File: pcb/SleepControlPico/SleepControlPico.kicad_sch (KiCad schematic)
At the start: 24 parts, among them J1 USB_C_Receptacle_PowerOnly_6P, J3 UART, J4 FFC2B35-18-G_REVA2, SW1 RotaryEncoder_Switch, SW2 SW_Push, U1 AMS1117-33, U2 ESP32-WROOM-32D, U3 LIS3DH

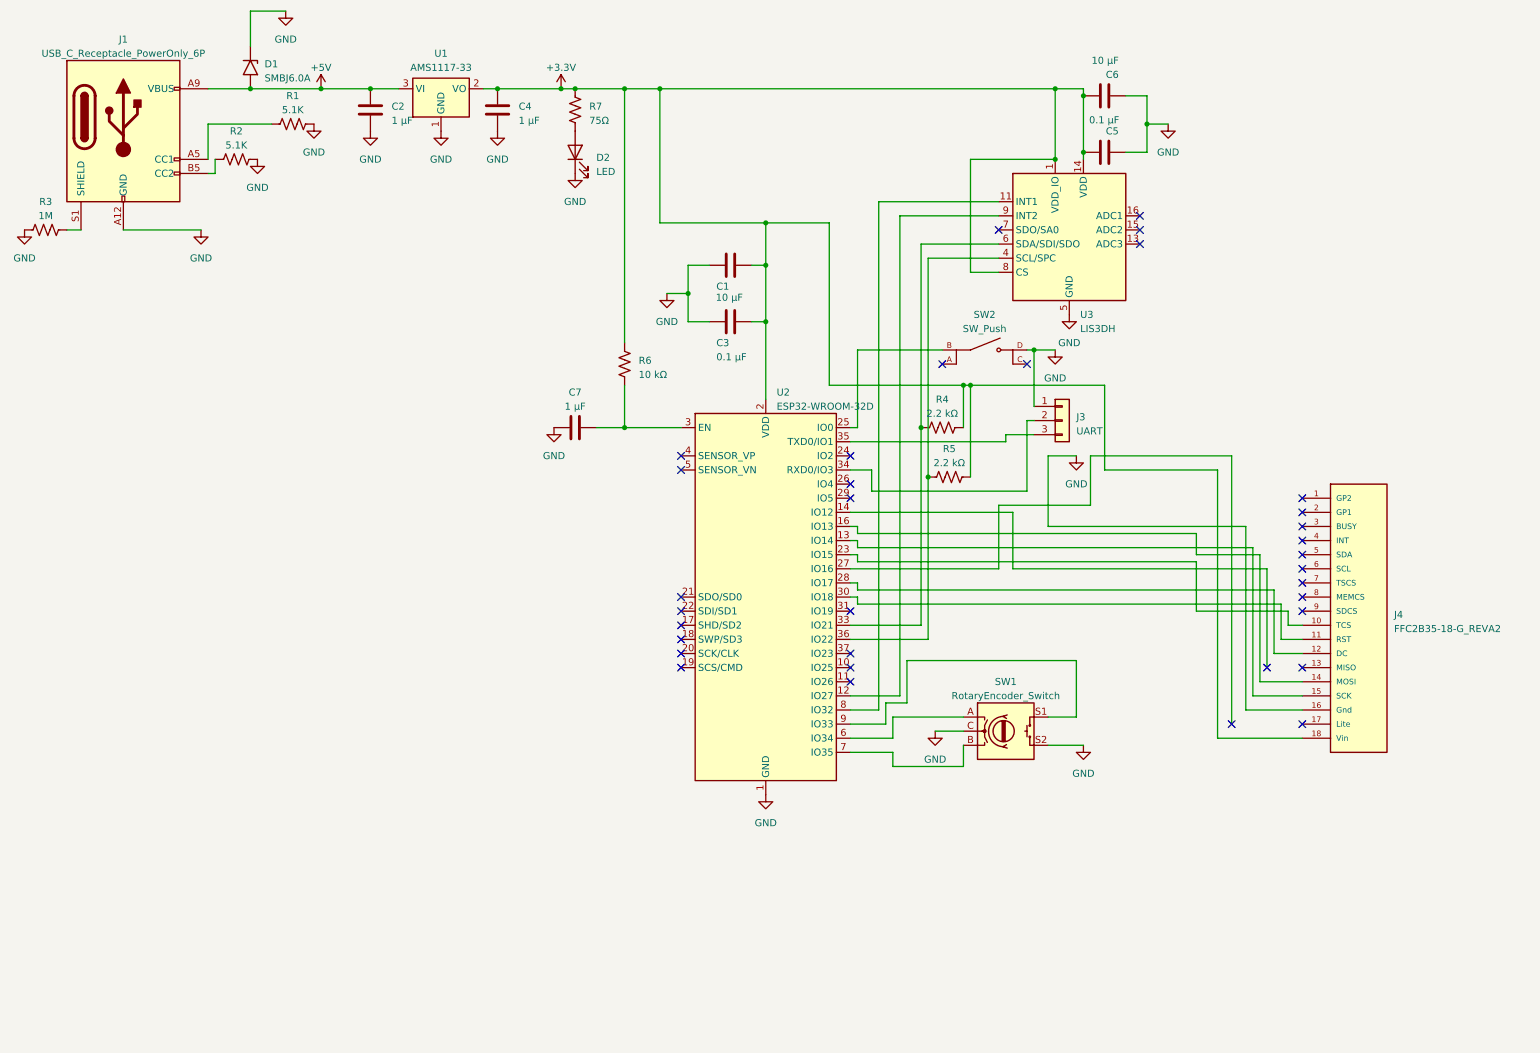
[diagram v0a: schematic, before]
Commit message: Smaller PCB using an ESP32-S3-MINI-1.
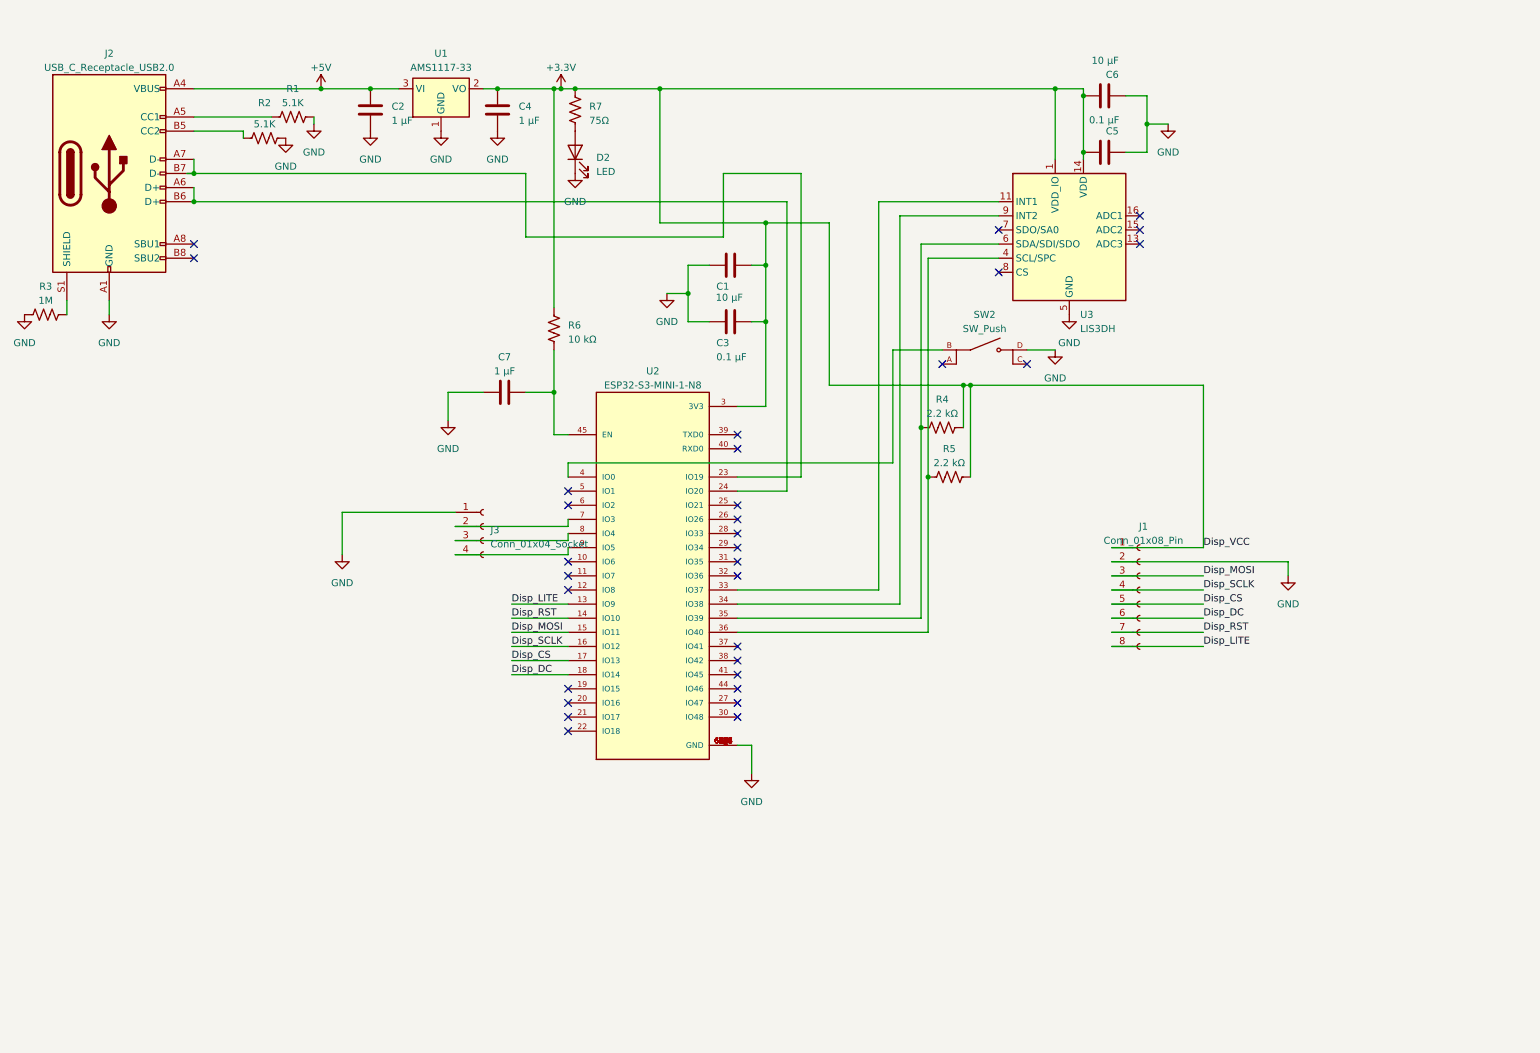
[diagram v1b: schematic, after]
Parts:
- removed D1: SMBJ6.0A, Diode_SMD:D_SMB, symbol Diode:SM6T56A
- removed J1: USB_C_Receptacle_PowerOnly_6P, Connector_USB:USB_C_Receptacle_G-Switch_GT-USB-7002C, symbol Connector:USB_C_Receptacle_PowerOnly_6P
- removed J3: UART, Connector_PinHeader_2.54mm:PinHeader_1x03_P2.54mm_Vertical, symbol Connector_Generic:Conn_01x03
- removed J4: FFC2B35-18-G_REVA2, Connector_FFC-FPC:Jushuo_AFC07_S18FCC, symbol FFC2B35-18-G_REVA2:FFC2B35-18-G_REVA2
- removed SW1: RotaryEncoder_Switch, eec:Bourns-PEC11R-4020F-S0012-MFG, symbol Device:RotaryEncoder_Switch
- removed U2: ESP32-WROOM-32D, RF_Module:ESP32-WROOM-32D, symbol RF_Module:ESP32-WROOM-32D
- added J1: Conn_01x08_Pin, Connector_JST:JST_PH_B8B-PH-K_1x08_P2.00mm_Vertical, symbol Connector:Conn_01x08_Socket
- added J2: USB_C_Receptacle_USB2.0, Connector_USB:USB_C_Receptacle_G-Switch_GT-USB-7010ASV, symbol Connector:USB_C_Receptacle_USB2.0
- added J3: Conn_01x04_Socket, Connector_JST:JST_PH_B4B-PH-K_1x04_P2.00mm_Vertical, symbol Connector:Conn_01x04_Socket
- added U2: ESP32-S3-MINI-1-N8, ESP32-S3-MINI-1-N8:XCVR_ESP32-S3-MINI-1-N8, symbol ESP32-S3-MINI-1-N8:ESP32-S3-MINI-1-N8
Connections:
- net +3.3V: now also J1.1 (Pin_1), U2.3 (3V3); no longer U3.8 (CS)
- net +5V: now also J2.A4 (VBUS), J2.A9 (VBUS), J2.B4 (VBUS), J2.B9 (VBUS)
- net GND: now also J1.2 (Pin_2), J2.A1 (GND), J2.A12 (GND), J2.B1 (GND), J2.B12 (GND), J3.1 (Pin_1), U2.1 (GND), U2.2 (GND), U2.42 (GND), U2.43 (GND), U2.46 (GND), U2.47 (GND), U2.48 (GND), U2.49 (GND), U2.50 (GND), U2.51 (GND), U2.52 (GND), U2.53 (GND), U2.54 (GND), U2.55 (GND), U2.56 (GND), U2.57 (GND), U2.58 (GND), U2.59 (GND), U2.60 (GND), U2.61 (GND), U2.61_1 (GND), U2.61_2 (GND), U2.61_3 (GND), U2.61_4 (GND), U2.61_5 (GND), U2.61_6 (GND), U2.61_7 (GND), U2.61_8 (GND), U2.62 (GND), U2.63 (GND), U2.64 (GND), U2.65 (GND)
- net at U3.9 (INT2): now also U2.34 (IO38)
- net at SW2.B: now also U2.4 (IO0)
- net at C7.2, R6.2: now also U2.45 (EN)
- net at R4.2, U3.6 (SDA/SDI/SDO): now also U2.35 (IO39)
- net at R5.1, U3.4 (SCL/SPC): now also U2.36 (IO40)
- net at U3.11 (INT1): now also U2.33 (IO37)
- net at R2.1: now also J2.B5 (CC2)
- net at R1.1: now also J2.A5 (CC1)
- net at R3.1: now also J2.S1 (SHIELD)
- new net: J3.2 (Pin_2), U2.7 (IO3)
- new net: J3.3 (Pin_3), U2.8 (IO4)
- new net: J3.4 (Pin_4), U2.9 (IO5)
- new net: J2.A7 (D-), J2.B7 (D-), U2.23 (IO19)
- new net: J2.A6 (D+), J2.B6 (D+), U2.24 (IO20)
- new net Disp_CS: J1.5 (Pin_5), U2.17 (IO13)
- new net Disp_DC: J1.6 (Pin_6), U2.18 (IO14)
- new net Disp_LITE: J1.8 (Pin_8), U2.13 (IO9)
- new net Disp_MOSI: J1.3 (Pin_3), U2.15 (IO11)
- new net Disp_RST: J1.7 (Pin_7), U2.14 (IO10)
- new net Disp_SCLK: J1.4 (Pin_4), U2.16 (IO12)
- no-connect marks 34 -> 32
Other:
- moved on the sheet: C7, R1, R2, R3, R6

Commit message: Final-ish PCB layout
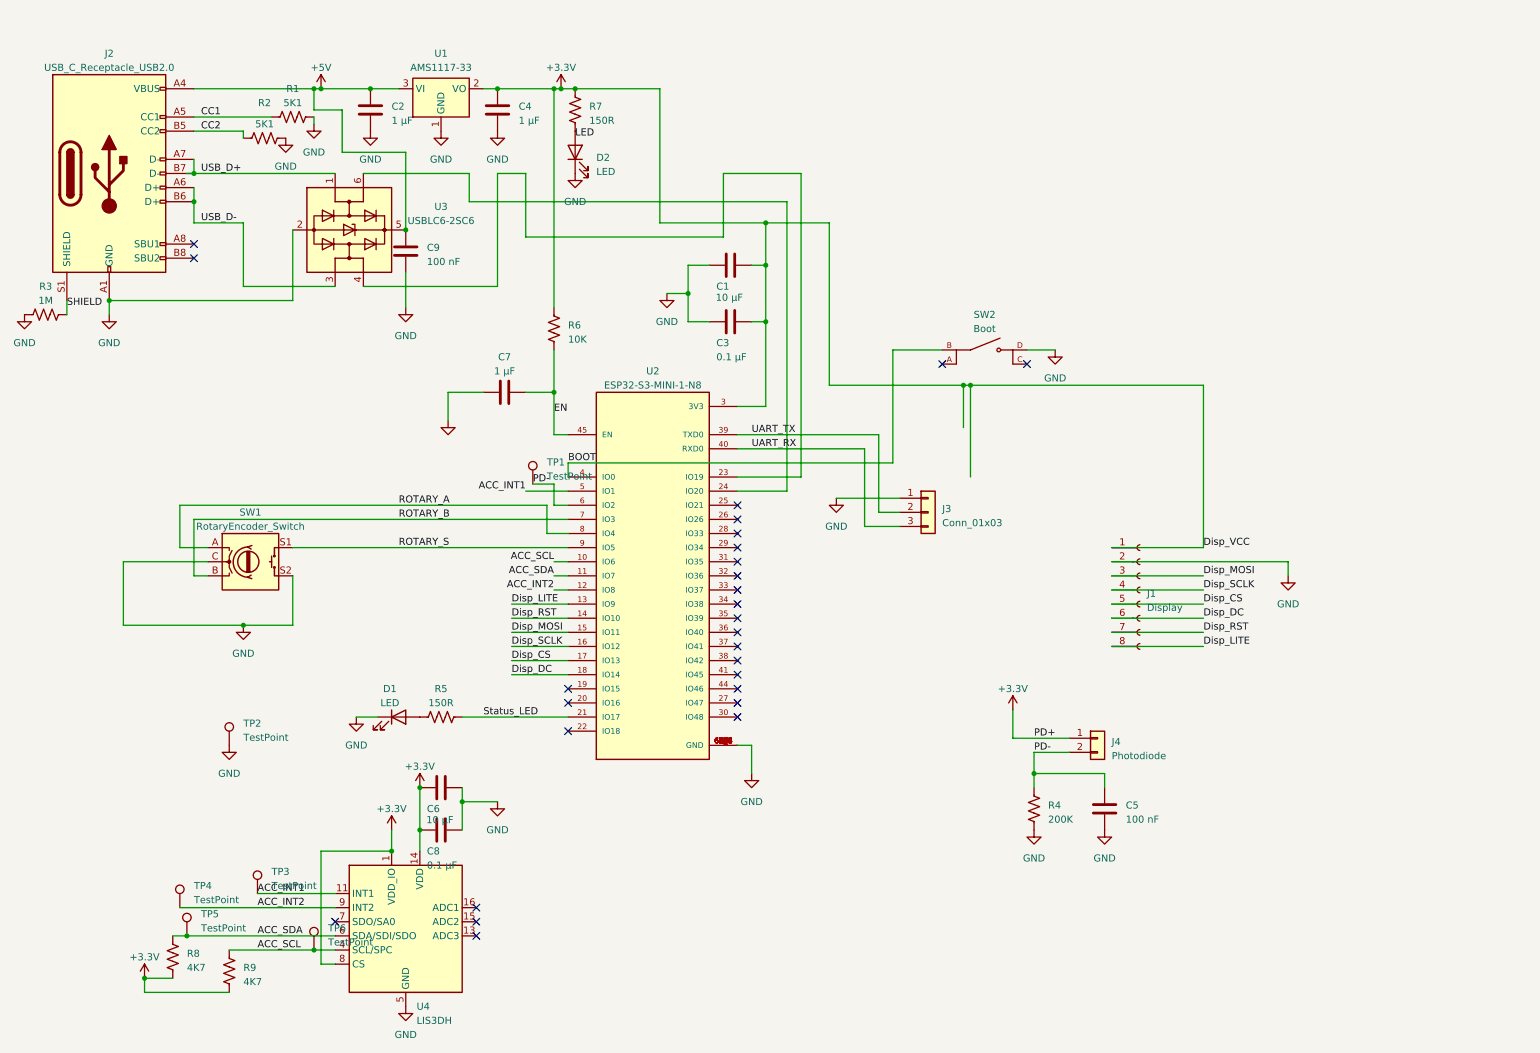
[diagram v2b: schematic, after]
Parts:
- removed J3: Conn_01x04_Socket, Connector_JST:JST_PH_B4B-PH-K_1x04_P2.00mm_Vertical, symbol Connector:Conn_01x04_Socket
- removed U3: LIS3DH, Package_LGA:LGA-16_3x3mm_P0.5mm_LayoutBorder3x5y, symbol Sensor_Motion:LIS3DH
- added C8: 0.1 µF, Capacitor_SMD:C_0402_1005Metric, symbol Device:C
- added C9: 100 nF, Capacitor_SMD:C_0402_1005Metric, symbol Device:C
- added D1: LED, LED_SMD:LED_0603_1608Metric, symbol Device:LED
- added J3: Conn_01x03, Connector_PinHeader_2.54mm:PinHeader_1x03_P2.54mm_Horizontal, symbol Connector_Generic:Conn_01x03
- added J4: Photodiode, Connector_JST:JST_PH_B2B-PH-K_1x02_P2.00mm_Vertical, symbol Connector_Generic:Conn_01x02
- added R8, R9: 4K7, Resistor_SMD:R_0603_1608Metric, symbol Device:R_US
- added SW1: RotaryEncoder_Switch, eec:Bourns-PEC11R-4020F-S0012-MFG, symbol Device:RotaryEncoder_Switch
- added TP1, TP2, TP3, TP4, TP5, TP6: TestPoint, TestPoint:TestPoint_Pad_D1.0mm, symbol Connector:TestPoint
- added U3: USBLC6-2SC6, Package_TO_SOT_SMD:SOT-23-6, symbol Power_Protection:USBLC6-2SC6
- added U4: LIS3DH, Package_LGA:LGA-16_3x3mm_P0.5mm_LayoutBorder3x5y, symbol Sensor_Motion:LIS3DH
- C5: value 0.1 µF -> 100 nF
- J1: value Conn_01x08_Pin -> Display; footprint Connector_JST:JST_PH_B8B-PH-K_1x08_P2.00mm_Vertical -> JST B8B-ZR:JST-B8B-ZR-0; LCSC Part # (none) -> C493145
- J2: LCSC Part # (none) -> C2988369
- R1, R2: value 5.1K -> 5K1
- R4: value 2.2 kΩ -> 200K; footprint Resistor_SMD:R_0603_1608Metric -> Resistor_THT:R_Axial_DIN0207_L6.3mm_D2.5mm_P7.62mm_Horizontal; LCSC Part # C4190 -> C58614
- R5: value 2.2 kΩ -> 150R; footprint Resistor_SMD:R_0603_1608Metric -> Resistor_SMD:R_0402_1005Metric; LCSC Part # C4190 -> C25133
- R6: value 10 kΩ -> 10K
- R7: value 75Ω -> 150R
- SW2: value SW_Push -> Boot
- U2: LCSC Part # (none) -> C2913206
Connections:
- net +3.3V: now also C6.2, C8.2, J4.1 (Pin_1), R8.2, R9.2, U4.1 (VDD_IO), U4.14 (VDD), U4.8 (CS); no longer C5.1, C6.1, R4.1, R5.2
- net +5V: now also C9.2, U3.5 (VBUS)
- net GND: now also C5.1, C6.1, R4.2, C8.1, C9.1, D1.1 (K), J3.1 (Pin_1), SW1.C, SW1.S2, TP2.1, U3.2 (GND), U4.10 (GND), U4.12 (GND), U4.5 (GND); no longer C5.2, C6.2
- net ROTARY_B: now reaches U2.7 (IO3)
- net ROTARY_B: now also SW1.B
- net ROTARY_A: now reaches U2.8 (IO4)
- net ROTARY_A: now also SW1.A
- net ROTARY_S: now reaches U2.9 (IO5)
- net ROTARY_S: now also SW1.S1
- net at U2.35 (IO39): no longer R4.2
- net CC2: now reaches J2.B5 (CC2), R2.1
- net CC1: now reaches J2.A5 (CC1), R1.1
- net ACC_SCL: now reaches U2.10 (IO6)
- net ACC_SCL: now also R9.1, TP6.1, U4.4 (SCL/SPC)
- net ACC_SDA: now reaches U2.11 (IO7)
- net ACC_SDA: now also R8.1, TP5.1, U4.6 (SDA/SDI/SDO)
- net ACC_INT2: now reaches U2.12 (IO8)
- net ACC_INT2: now also TP4.1, U4.9 (INT2)
- net Status_LED: now reaches U2.21 (IO17)
- net Status_LED: now also R5.2
- net USB_D+: now reaches J2.A7 (D-), J2.B7 (D-)
- net USB_D+: now also U3.1 (I/O1); no longer U2.23 (IO19)
- net USB_D-: now reaches J2.A6 (D+), J2.B6 (D+)
- net USB_D-: now also U3.3 (I/O2); no longer U2.24 (IO20)
- net at R5.1: now also D1.2 (A); no longer U2.36 (IO40)
- net UART_TX: now reaches U2.39 (TXD0)
- net UART_TX: now also J3.2 (Pin_2)
- net BOOT: now reaches SW2.B, U2.4 (IO0)
- net UART_RX: now reaches U2.40 (RXD0)
- net UART_RX: now also J3.3 (Pin_3)
- net EN: now reaches C7.2, R6.2, U2.45 (EN)
- net ACC_INT1: now reaches U2.5 (IO1)
- net ACC_INT1: now also TP3.1, U4.11 (INT1)
- net PD-: now reaches U2.6 (IO2)
- net PD-: now also C5.2, R4.1, J4.2 (Pin_2), TP1.1
- net SHIELD: now reaches J2.S1 (SHIELD), R3.1
- new net: U2.23 (IO19), U3.4 (I/O2)
- new net: U2.24 (IO20), U3.6 (I/O1)
- no-connect marks 32 -> 27

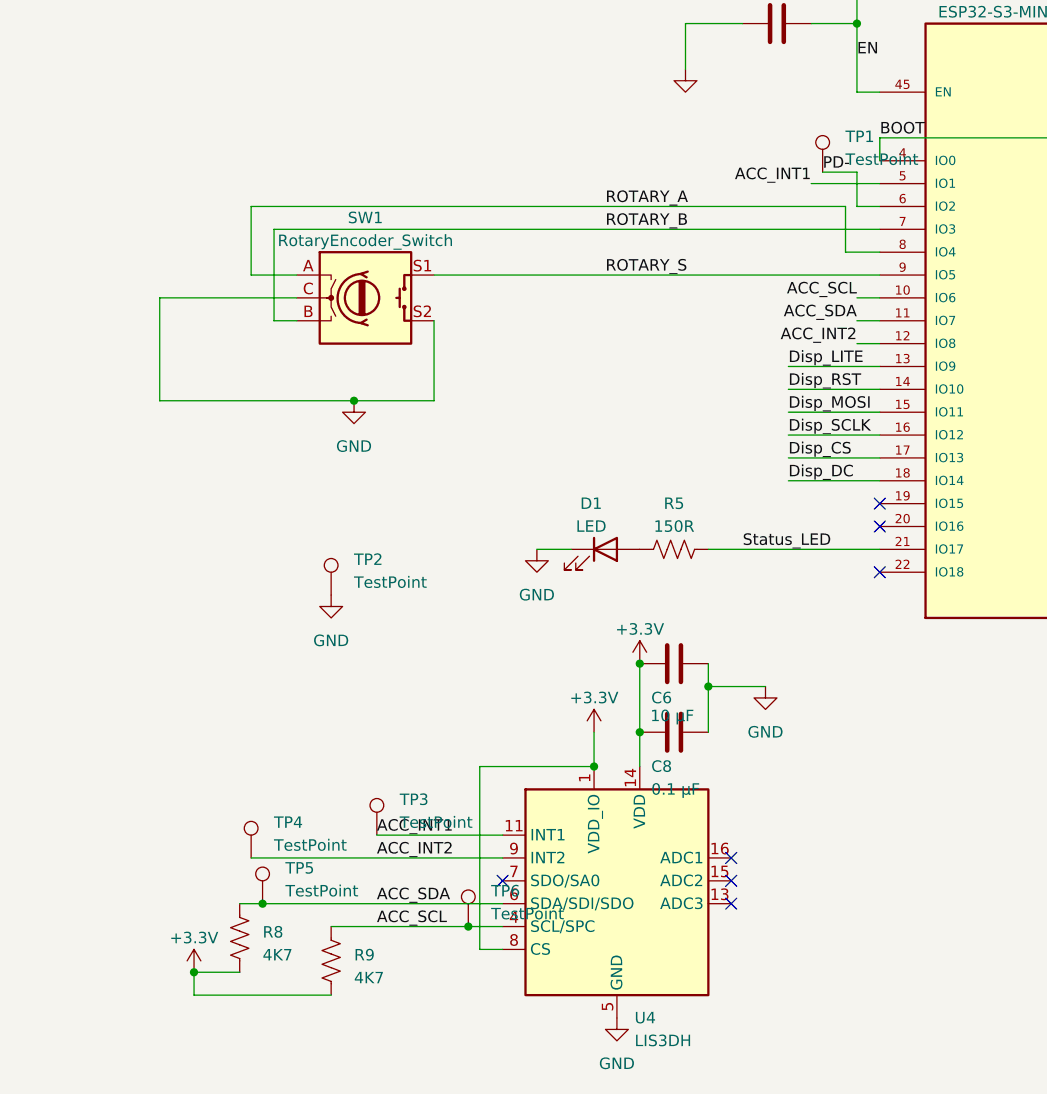
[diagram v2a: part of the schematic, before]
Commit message: remove accelerometer (out of stock)
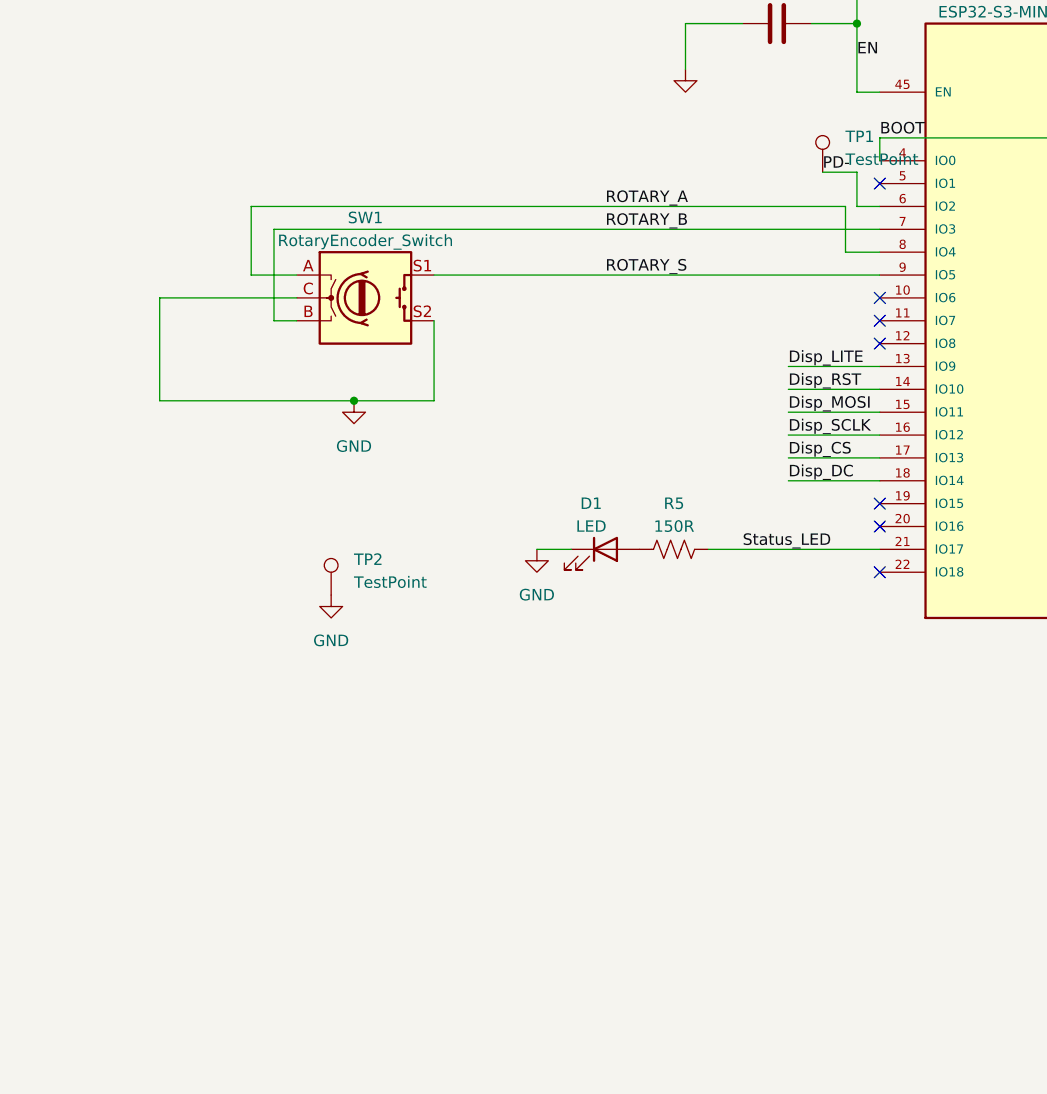
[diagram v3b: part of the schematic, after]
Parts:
- removed C6: 10 µF, Capacitor_SMD:C_0603_1608Metric, symbol Device:C
- removed C8: 0.1 µF, Capacitor_SMD:C_0402_1005Metric, symbol Device:C
- removed R8, R9: 4K7, Resistor_SMD:R_0603_1608Metric, symbol Device:R_US
- removed TP3, TP4, TP5, TP6: TestPoint, TestPoint:TestPoint_Pad_D1.0mm, symbol Connector:TestPoint
- removed U4: LIS3DH, Package_LGA:LGA-16_3x3mm_P0.5mm_LayoutBorder3x5y, symbol Sensor_Motion:LIS3DH
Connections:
- net ACC_INT1: no longer names the net of U2.5 (IO1)
- net ACC_INT2: no longer names the net of U2.12 (IO8)
- net ACC_SCL: no longer names the net of U2.10 (IO6)
- net ACC_SDA: no longer names the net of U2.11 (IO7)

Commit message: Final(?) PCB revision.
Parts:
- R7: LCSC Part # C25133 -> C25082
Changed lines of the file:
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@@
       (effects (font (size 1.27 1.27)) hide)
     )
-    (property "LCSC Part #" "C25133" (at 119.38 33.02 0)
+    (property "LCSC Part #" "C25082" (at 119.38 33.02 0)
       (effects (font (size 1.27 1.27)) hide)
     )
